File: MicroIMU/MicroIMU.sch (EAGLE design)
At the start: 17 parts

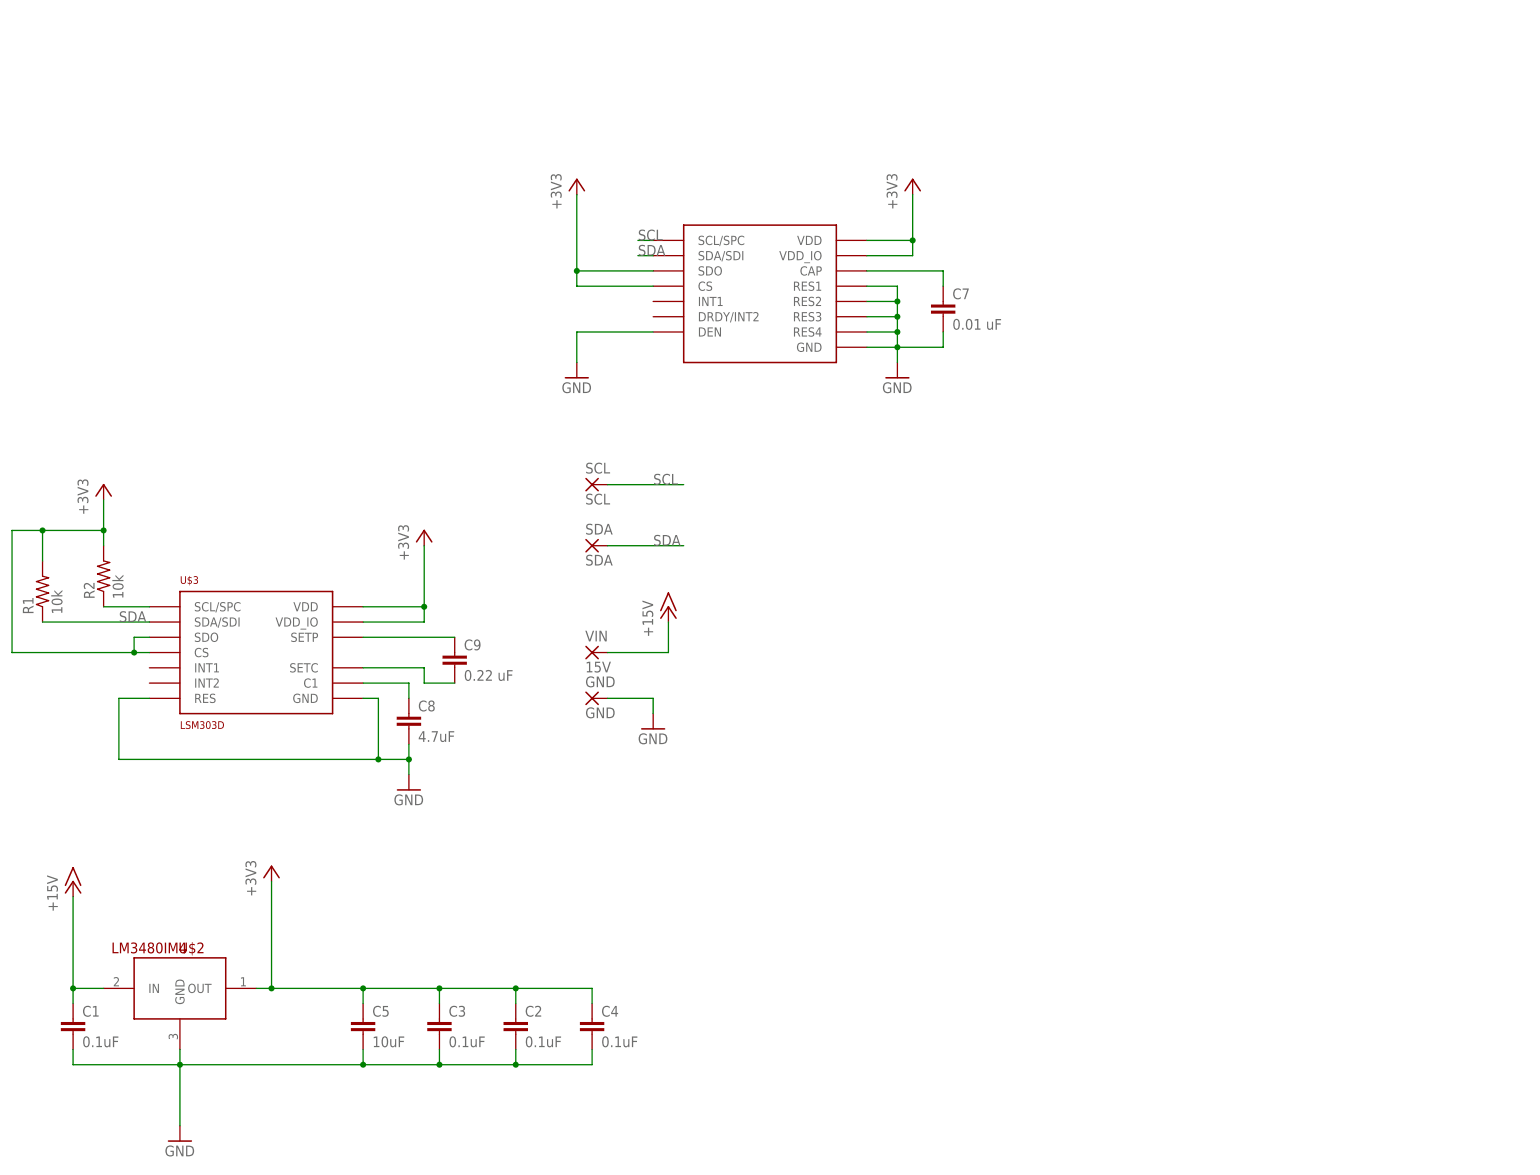
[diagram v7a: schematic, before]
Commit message: changed to invense MPU9250
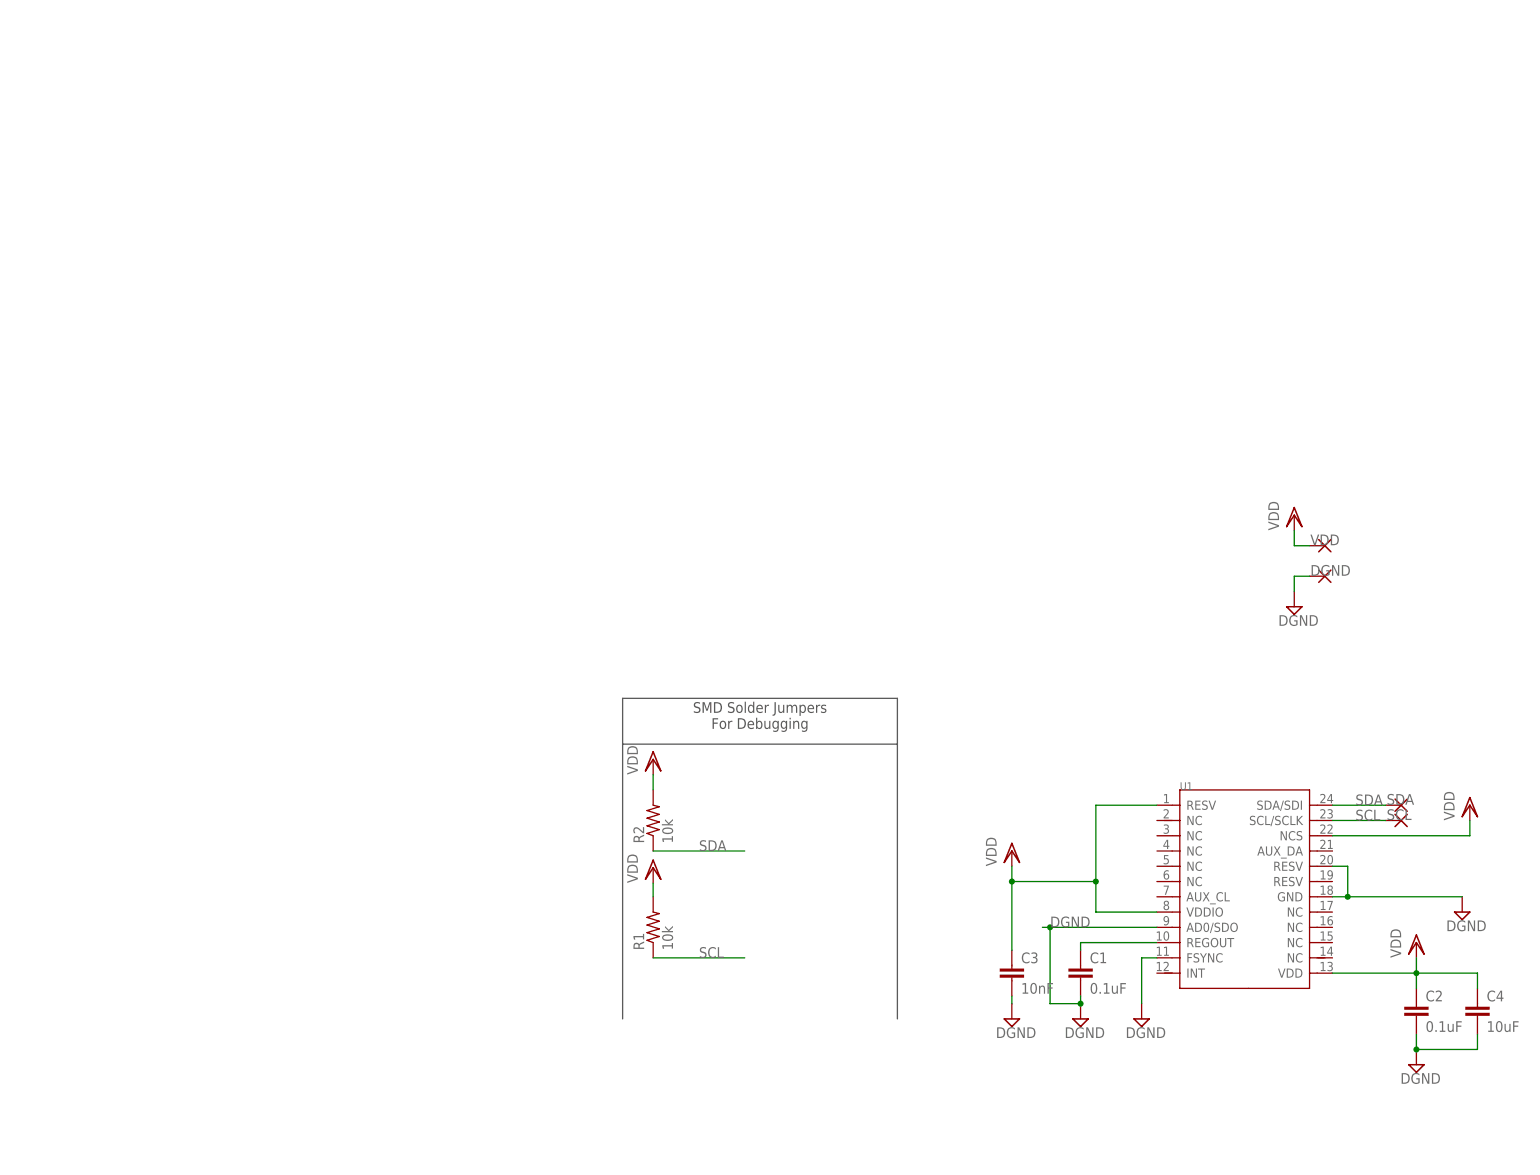
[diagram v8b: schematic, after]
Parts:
- removed C5: 10uF, resistor:C-EUC0603
- removed C7: 0.01 uF, resistor:C-EUC0402
- removed C8: 4.7uF, resistor:C-EUC0402
- removed C9: 0.22 uF, resistor:C-EUC0201
- removed GND: GND, wirepad:1,6/0,8
- removed U$1: L3GD20H, st:L3GD20H
- removed U$2: LM3480IM4, SparkFun-PowerIC:LM3480IM4
- removed U$3: LSM303D, st:LSM303D
- removed VIN: 15V, wirepad:1,6/0,8
- added DGND, VDD: (no value), michael-stetner:THROUGH-HOLE-30MIL/15MIL
- added U1: (no value), Grove - IMU 10DOF v1.1:MPU-9250
- C1, C2: device resistor:C-EUC0201 -> resistor:C-EUC0402
- C3: value 0.1uF -> 10nF; device resistor:C-EUC0201 -> resistor:C-EUC0402
- C4: value 0.1uF -> 10uF; device resistor:C-EUC0201 -> resistor:C-EUC0603
- SCL: value SCL -> (none); device wirepad:1,6/0,8 -> michael-stetner:THROUGH-HOLE-30MIL/15MIL
- SDA: value SDA -> (none); device wirepad:1,6/0,8 -> michael-stetner:THROUGH-HOLE-30MIL/15MIL
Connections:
- removed net +15V: C1.1, U$2.IN, VIN.P
- removed net +3V3: C2.1, C3.1, C4.1, C5.1, R1.2, R2.2, U$1.CS, U$1.SDO, U$1.VDD, U$1.VDD_IO, U$2.OUT, U$3.CS, U$3.SDO, U$3.VDD, U$3.VDD_IO
- removed net GND: C1.2, C2.2, C3.2, C4.2, C5.2, C7.2, C8.2, GND.P, U$1.DEN, U$1.GND, U$1.RES1, U$1.RES2, U$1.RES3, U$1.RES4, U$2.GND, U$3.GND, U$3.RES
- removed net N$1: C8.1, U$3.C1
- removed net N$2: C9.1, U$3.SETP
- removed net N$3: C9.2, U$3.SETC
- removed net N$9: C7.1, U$1.CAP
- new net DGND: C1.2, C2.2, C3.2, C4.2, DGND.P, U1.AD0/SDO, U1.FSYNC, U1.GND, U1.RESV@2
- new net N$7: C1.1, U1.REGOUT
- new net VDD: C2.1, C3.1, C4.1, R1.2, R2.2, U1.NCS, U1.RESV, U1.VDD, U1.VDDIO, VDD.P
- net SCL: now also R1.1, U1.SCL/SCLK; no longer R2.1, U$1.SCL/SPC, U$3.SCL/SPC
- net SDA: now also R2.1, U1.SDA/SDI; no longer R1.1, U$1.SDA/SDI, U$3.SDA/SDI
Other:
- note added: "SMD Solder Jumpers For Debugging"
- moved on the sheet: C1, C2, C3, C4, R1, R2, SCL, SDA
